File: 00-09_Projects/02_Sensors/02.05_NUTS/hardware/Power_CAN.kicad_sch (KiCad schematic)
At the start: 21 parts, among them J2 USB_C_Receptacle_USB2.0_16P, J3 Conn_01x04_Socket, U1 SN65HVD230, U3 LM3940IMP-3.3/NOPB

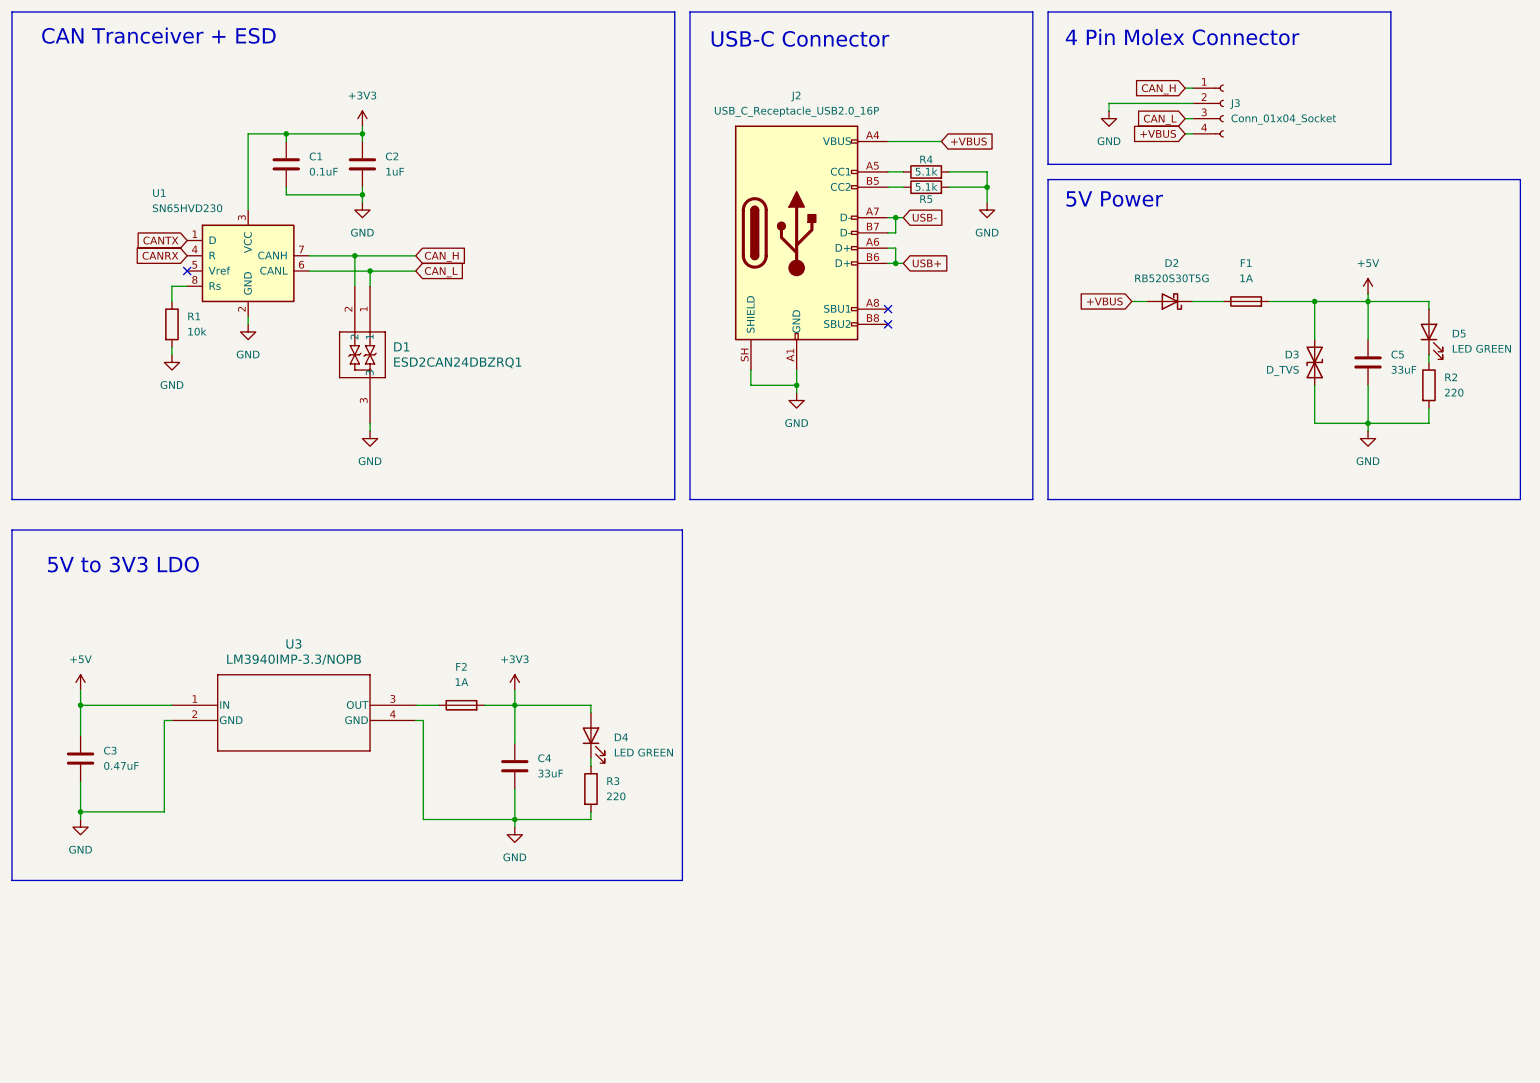
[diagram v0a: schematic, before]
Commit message: Design review changes
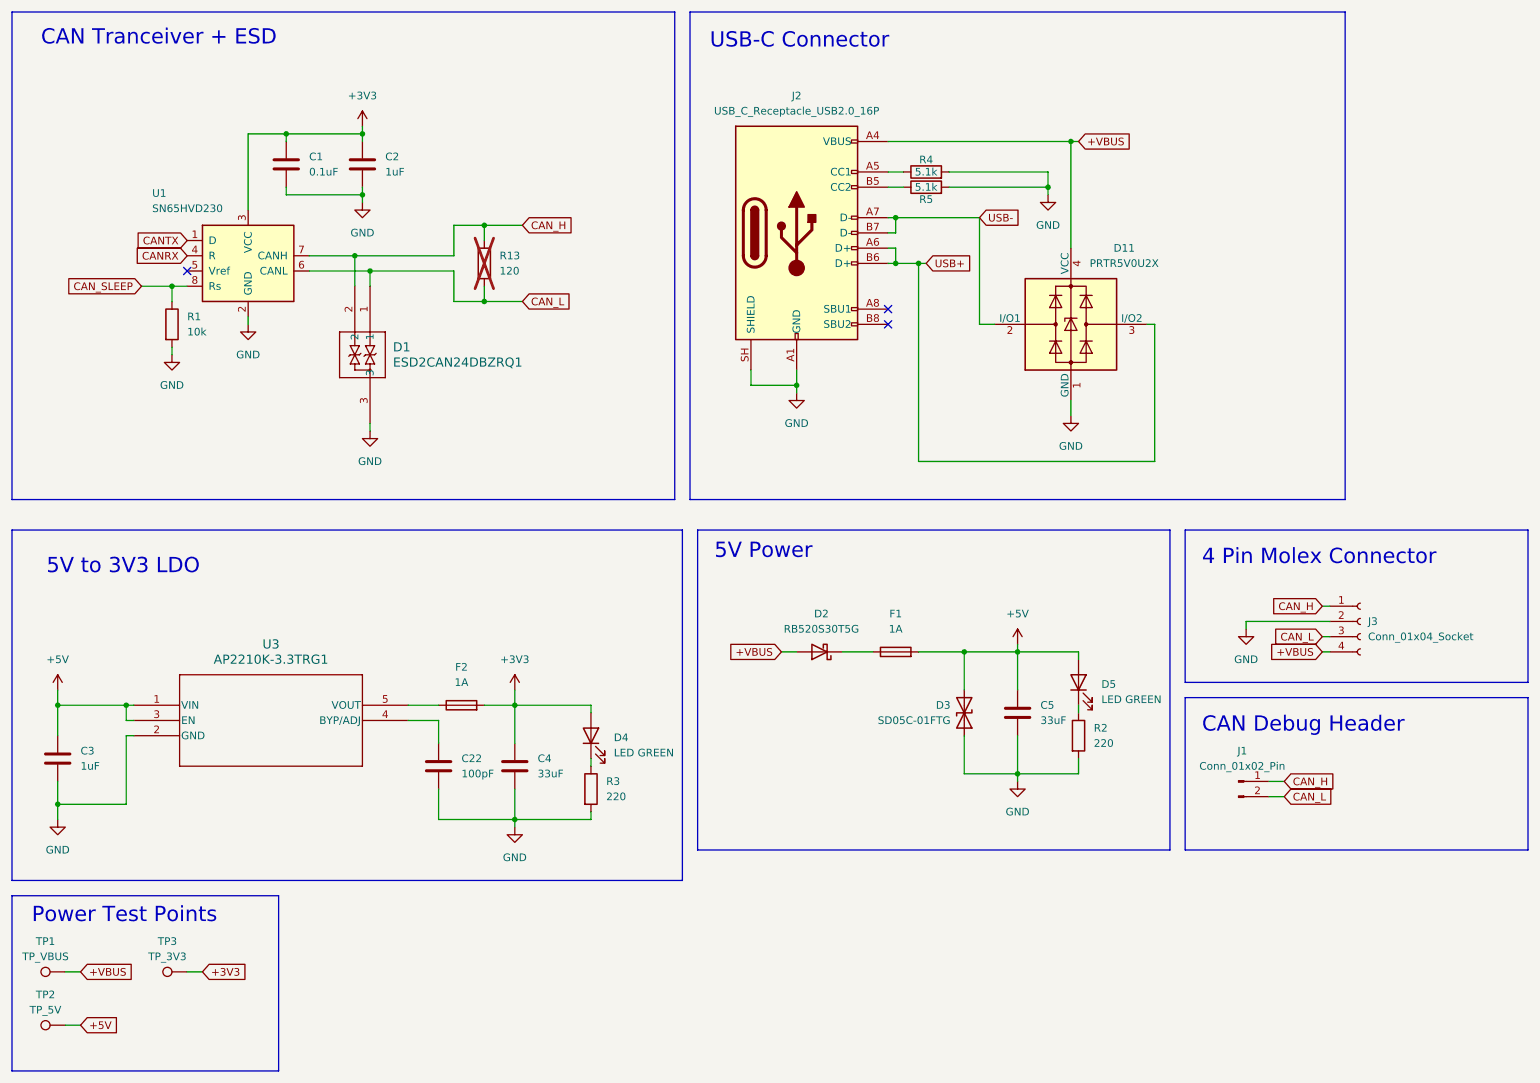
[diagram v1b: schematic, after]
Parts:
- removed U3: LM3940IMP-3.3/NOPB, MP04A, symbol Undertray_Board_sym:LM3940IMP-3.3_NOPB
- added C22: 100pF, Capacitor_SMD:C_0805_2012Metric_Pad1.18x1.45mm_HandSolder, symbol Device:C
- added D11: PRTR5V0U2X, Package_TO_SOT_SMD:SOT-143, symbol Power_Protection:PRTR5V0U2X
- added J1: Conn_01x02_Pin, symbol Connector:Conn_01x02_Pin
- added R13: 120, symbol Device:R
- added TP1: TP_VBUS, symbol Connector:TestPoint
- added TP2: TP_5V, symbol Connector:TestPoint
- added TP3: TP_3V3, symbol Connector:TestPoint
- added U3: AP2210K-3.3TRG1, SOT-23-5_DIO, symbol Undertray_Board_sym:AP2210K-3.3TRG1
- C3: value 0.47uF -> 1uF
- D3: value D_TVS -> SD05C-01FTG
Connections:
- net +3V3: now also TP3.1
- net +5V: now also TP2.1, U3.1 (VIN), U3.3 (EN)
- net +VBUS: now also D11.4 (VCC), TP1.1
- net CAN_H: now also J1.1 (Pin_1), R13.1
- net CAN_L: now also J1.2 (Pin_2), R13.2
- net GND: now also C22.2, D11.1 (GND), U3.2 (GND)
- net USB+: now also D11.3 (I/O2)
- net USB-: now also D11.2 (I/O1)
- net at F2.1: now also U3.5 (VOUT)
- net CAN_SLEEP: now reaches R1.1, U1.8 (Rs)
- new net: C22.1, U3.4 (BYP/ADJ)
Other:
- note added: "CAN Debug Header"
- note added: "Power Test Points"
- moved on the sheet: C3, C5, D2, D3, D5, F1, J3, R2

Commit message: Rev A layout done
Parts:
- removed J1: Conn_01x02_Pin, symbol Connector:Conn_01x02_Pin
- removed J2: USB_C_Receptacle_USB2.0_16P, symbol Connector:USB_C_Receptacle_USB2.0_16P
- added J1: USB_C_Receptacle_USB2.0_16P, Connector_USB:USB_C_Receptacle_XKB_U262-16XN-4BVC11, symbol Connector:USB_C_Receptacle_USB2.0_16P
- D1: footprint SOT-23_DBZ_TEX -> Package_TO_SOT_SMD:SC-59_Handsoldering
- D2: footprint (none) -> Diode_SMD:D_SOD-523
- D3: footprint (none) -> Diode_SMD:D_SOD-323_HandSoldering
- F1, F2: value 1A -> 750mA; footprint (none) -> Fuse:Fuse_1206_3216Metric_Pad1.42x1.75mm_HandSolder
- J3: footprint (none) -> Undertray FP:CONN_SD-43045-001_04_MOL
- R13: footprint (none) -> Resistor_SMD:R_0603_1608Metric_Pad0.98x0.95mm_HandSolder
- TP1, TP2, TP3: footprint (none) -> TestPoint:TestPoint_THTPad_D1.5mm_Drill0.7mm
- U3: footprint SOT-23-5_DIO -> Package_TO_SOT_SMD:SOT-23-5_HandSoldering
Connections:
- net +VBUS: now also J3.2 (Pin_2), J1.A4 (VBUS), J1.A9 (VBUS), J1.B4 (VBUS), J1.B9 (VBUS); no longer J3.4 (Pin_4)
- net CAN_H: now also J3.3 (Pin_3); no longer J3.1 (Pin_1)
- net CAN_L: now also J3.4 (Pin_4); no longer J3.3 (Pin_3)
- net GND: now also J3.1 (Pin_1), J1.A1 (GND), J1.A12 (GND), J1.B1 (GND), J1.B12 (GND), J1.SH (SHIELD); no longer J3.2 (Pin_2)
- net USB+: now also J1.A6 (D+), J1.B6 (D+)
- net USB-: now also J1.A7 (D-), J1.B7 (D-)
- net at R5.1: now also J1.B5 (CC2)
- net at R4.1: now also J1.A5 (CC1)
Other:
- note removed: "CAN Debug Header"

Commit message: Design review rev 1 changes
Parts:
- renumbered C5 to C3, C3 to C4, C22 to C5, C4 to C6, D11 to D2, D2 to D3, D5 to D4, D3 to D5, D4 to D6, J3 to J2, R4 to R1, R5 to R2, R13 to R3, R1 to R4, R2 to R5, R3 to R6, TP3 to TP2, TP2 to TP3, U3 to U2

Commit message: last changes
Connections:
- net +VBUS: now also J2.1 (Pin_1); no longer J2.2 (Pin_2)
- net GND: now also J2.2 (Pin_2); no longer J2.1 (Pin_1)
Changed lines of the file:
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@@
 	(wire
 		(pts
-			(xy 223.52 115.57) (xy 237.49 115.57)
-		)
-		(stroke
-			(width 0)
-			(type default)
-		)
-	)
-	(wire
-		(pts
 			(xy 176.53 137.16) (xy 176.53 143.51)
 		)
@@
 	(wire
 		(pts
-			(xy 236.22 118.11) (xy 237.49 118.11)
-		)
-		(stroke
-			(width 0)
-			(type default)
-		)
-	)
-	(wire
-		(pts
 			(xy 63.5 36.83) (xy 76.2 36.83)
 		)
@@
 	(wire
 		(pts
+			(xy 222.25 118.11) (xy 222.25 119.38)
+		)
+		(stroke
+			(width 0)
+			(type default)
+		)
+	)
+	(wire
+		(pts
 			(xy 25.4 132.08) (xy 36.83 132.08)
 		)
@@
 	(wire
 		(pts
+			(xy 222.25 118.11) (xy 237.49 118.11)
+		)
+		(stroke
+			(width 0)
+			(type default)
+		)
+	)
+	(wire
+		(pts
 			(xy 36.83 134.62) (xy 36.83 132.08)
 		)
@@
 	(wire
 		(pts
-			(xy 223.52 115.57) (xy 223.52 116.84)
-		)
-		(stroke
-			(width 0)
-			(type default)
-		)
-	)
-	(wire
-		(pts
 			(xy 63.5 36.83) (xy 63.5 38.1)
 		)
@@
 	(wire
 		(pts
+			(xy 236.22 115.57) (xy 237.49 115.57)
+		)
+		(stroke
+			(width 0)
+			(type default)
+		)
+	)
+	(wire
+		(pts
 			(xy 101.6 129.54) (xy 101.6 132.08)
 		)
@@
 		)
 	)
-	(global_label "+VBUS"
+	(global_label "CAN_L"
 		(shape input)
-		(at 236.22 118.11 180)
+		(at 236.22 123.19 180)
 		(fields_autoplaced yes)
 		(effects
@@
 		)
 		(property "Intersheetrefs" "${INTERSHEET_REFS}"
-			(at 226.7638 118.11 0)
+			(at 227.55 123.19 0)
 			(hide yes)
 			(show_name no)
@@
 		)
 	)
-	(global_label "CAN_L"
+	(global_label "+VBUS"
 		(shape input)
-		(at 236.22 123.19 180)
+		(at 236.22 115.57 180)
 		(fields_autoplaced yes)
 		(effects
@@
 		)
 		(property "Intersheetrefs" "${INTERSHEET_REFS}"
-			(at 227.55 123.19 0)
+			(at 226.7638 115.57 0)
 			(hide yes)
 			(show_name no)
@@
 	)
 	(symbol
-		(lib_id "power:GND")
-		(at 223.52 116.84 0)
-		(mirror y)
-		(unit 1)
-		(body_style 1)
-		(exclude_from_sim no)
-		(in_bom yes)
-		(on_board yes)
-		(in_pos_files yes)
-		(dnp no)
-		(fields_autoplaced yes)
-		(property "Reference" "#PWR013"
-			(at 223.52 123.19 0)
-			(hide yes)
-			(show_name no)
-			(do_not_autoplace no)
-			(effects
-				(font
-					(size 1.27 1.27)
-				)
-			)
-		)
-		(property "Value" "GND"
-			(at 223.52 121.92 0)
-			(show_name no)
-			(do_not_autoplace no)
-			(effects
-				(font
-					(size 1.27 1.27)
-				)
-			)
-		)
-		(property "Footprint" ""
-			(at 223.52 116.84 0)
-			(hide yes)
-			(show_name no)
-			(do_not_autoplace no)
-			(effects
-				(font
-					(size 1.27 1.27)
-				)
-			)
-		)
-		(property "Datasheet" ""
-			(at 223.52 116.84 0)
-			(hide yes)
-			(show_name no)
-			(do_not_autoplace no)
-			(effects
-				(font
-					(size 1.27 1.27)
-				)
-			)
-		)
-		(property "Description" "Power symbol creates a global label with name \"GND\" , ground"
-			(at 223.52 116.84 0)
-			(hide yes)
-			(show_name no)
-			(do_not_autoplace no)
-			(effects
-				(font
-					(size 1.27 1.27)
-				)
-			)
-		)
-		(pin "1"
-		)
-		(instances
-			(project "Undertray_Board"
-				(path "/85866aa8-1074-44e2-a4f8-fc50fec0cbab/be2888db-2070-4339-a2b3-9cc9a585c76f"
-					(reference "#PWR013")
-					(unit 1)
-				)
-			)
-		)
-	)
-	(symbol
 		(lib_id "Device:C")
 		(at 185.42 133.35 0)
@@
 					(unit 1)
 				)
+			)
+		)
+	)
+	(symbol
+		(lib_id "power:GND")
+		(at 222.25 119.38 0)
+		(mirror y)
+		(unit 1)
+		(body_style 1)
+		(exclude_from_sim no)
+		(in_bom yes)
+		(on_board yes)
+		(in_pos_files yes)
+		(dnp no)
+		(fields_autoplaced yes)
+		(property "Reference" "#PWR013"
+			(at 222.25 125.73 0)
+			(hide yes)
+			(show_name no)
+			(do_not_autoplace no)
+			(effects
+				(font
+					(size 1.27 1.27)
+				)
+			)
+		)
+		(property "Value" "GND"
+			(at 222.25 124.46 0)
+			(show_name no)
+			(do_not_autoplace no)
+			(effects
+				(font
+					(size 1.27 1.27)
+				)
+			)
+		)
+		(property "Footprint" ""
+			(at 222.25 119.38 0)
+			(hide yes)
+			(show_name no)
+			(do_not_autoplace no)
+			(effects
+				(font
+					(size 1.27 1.27)
+				)
+			)
+		)
+		(property "Datasheet" ""
+			(at 222.25 119.38 0)
+			(hide yes)
+			(show_name no)
+			(do_not_autoplace no)
+			(effects
+				(font
+					(size 1.27 1.27)
+				)
+			)
+		)
+		(property "Description" "Power symbol creates a global label with name \"GND\" , ground"
+			(at 222.25 119.38 0)
+			(hide yes)
+			(show_name no)
+			(do_not_autoplace no)
+			(effects
+				(font
+					(size 1.27 1.27)
+				)
+			)
+		)
+		(pin "1"
+		)
+		(instances
+			(project "Undertray_Board"
+				(path "/85866aa8-1074-44e2-a4f8-fc50fec0cbab/be2888db-2070-4339-a2b3-9cc9a585c76f"
+					(reference "#PWR013")
+					(unit 1)
+				)

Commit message: extra changes
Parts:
- R5, R6: value 220 -> 330
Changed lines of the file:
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@@
 			)
 		)
-		(property "Value" "220"
+		(property "Value" "330"
 			(at 198.12 138.4299 0)
 			(show_name no)
@@
 			)
 		)
-		(property "Value" "220"
+		(property "Value" "330"
 			(at 116.84 147.3199 0)
 			(show_name no)

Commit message: solder jumper for reset
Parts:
- D3: value RB520S30T5G -> SDM20U30-7
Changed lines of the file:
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@@
 			)
 		)
-		(property "Value" "RB520S30T5G"
+		(property "Value" "SDM20U30-7"
 			(at 152.7175 119.38 0)
 			(show_name no)

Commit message: usb D+ pull up res fix
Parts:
- added R20: 1.5k, Resistor_SMD:R_0603_1608Metric_Pad0.98x0.95mm_HandSolder, symbol Device:R
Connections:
- net +3V3: now also R20.1
- net USB+: now also R20.2
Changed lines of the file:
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@@
 	)
 	(junction
+		(at 195.58 123.19)
+		(diameter 0)
+		(color 0 0 0 0)
+	)
+	(junction
 		(at 76.2 36.83)
 		(diameter 0)
@@
 	)
 	(junction
+		(at 214.63 68.58)
+		(diameter 0)
+		(color 0 0 0 0)
+	)
+	(junction
 		(at 25.4 148.59)
 		(diameter 0)
@@
 	)
 	(junction
-		(at 168.91 58.42)
+		(at 44.45 62.23)
 		(diameter 0)
 		(color 0 0 0 0)
 	)
 	(junction
-		(at 44.45 62.23)
+		(at 148.59 78.74)
 		(diameter 0)
 		(color 0 0 0 0)
 	)
 	(junction
-		(at 148.59 78.74)
+		(at 195.58 143.51)
 		(diameter 0)
 		(color 0 0 0 0)
@@
 	(wire
 		(pts
+			(xy 195.58 143.51) (xy 185.42 143.51)
+		)
+		(stroke
+			(width 0)
+			(type default)
+		)
+	)
+	(wire
+		(pts
 			(xy 38.1 134.62) (xy 36.83 134.62)
 		)
@@
 	(wire
 		(pts
-			(xy 208.28 68.58) (xy 207.01 68.58)
+			(xy 214.63 68.58) (xy 207.01 68.58)
 		)
 		(stroke
@@
 	(wire
 		(pts
-			(xy 185.42 144.78) (xy 185.42 143.51)
+			(xy 214.63 66.04) (xy 214.63 68.58)
 		)
 		(stroke
@@
 	(wire
 		(pts
-			(xy 25.4 144.78) (xy 25.4 148.59)
+			(xy 195.58 144.78) (xy 195.58 143.51)
 		)
 		(stroke
@@
 	(wire
 		(pts
-			(xy 38.1 137.16) (xy 36.83 137.16)
+			(xy 25.4 144.78) (xy 25.4 148.59)
 		)
 		(stroke
@@
 	(wire
 		(pts
-			(xy 170.18 58.42) (xy 168.91 58.42)
+			(xy 38.1 137.16) (xy 36.83 137.16)
 		)
 		(stroke
@@
 	(wire
 		(pts
-			(xy 208.28 91.44) (xy 168.91 91.44)
+			(xy 214.63 91.44) (xy 168.91 91.44)
 		)
 		(stroke
@@
 	(wire
 		(pts
+			(xy 214.63 54.61) (xy 214.63 58.42)
+		)
+		(stroke
+			(width 0)
+			(type default)
+		)
+	)
+	(wire
+		(pts
 			(xy 146.05 123.19) (xy 148.59 123.19)
 		)
@@
 	(wire
 		(pts
-			(xy 195.58 132.08) (xy 195.58 133.35)
+			(xy 214.63 68.58) (xy 215.9 68.58)
 		)
 		(stroke
@@
 	(wire
 		(pts
-			(xy 195.58 143.51) (xy 185.42 143.51)
+			(xy 195.58 132.08) (xy 195.58 133.35)
 		)
 		(stroke
@@
 	(wire
 		(pts
-			(xy 185.42 121.92) (xy 185.42 123.19)
+			(xy 195.58 120.65) (xy 195.58 123.19)
 		)
 		(stroke
@@
 	(wire
 		(pts
-			(xy 208.28 68.58) (xy 208.28 91.44)
+			(xy 214.63 68.58) (xy 214.63 91.44)
 		)
 		(stroke
@@
 		)
 	)
-	(global_label "USB+"
-		(shape input)
-		(at 170.18 58.42 0)
-		(fields_autoplaced yes)
-		(effects
-			(font
-				(size 1.27 1.27)
-			)
-			(justify left)
-		)
-		(property "Intersheetrefs" "${INTERSHEET_REFS}"
-			(at 178.5476 58.42 0)
-			(hide yes)
-			(show_name no)
-			(do_not_autoplace no)
-			(effects
-				(font
-					(size 1.27 1.27)
-				)
-				(justify left)
-			)
-		)
-	)
 	(global_label "CAN_SLEEP"
 		(shape input)
@@
 		)
 	)
+	(global_label "USB+"
+		(shape input)
+		(at 215.9 68.58 0)
+		(fields_autoplaced yes)
+		(effects
+			(font
+				(size 1.27 1.27)
+			)
+			(justify left)
+		)
+		(property "Intersheetrefs" "${INTERSHEET_REFS}"
+			(at 224.2676 68.58 0)
+			(hide yes)
+			(show_name no)
+			(do_not_autoplace no)
+			(effects
+				(font
+					(size 1.27 1.27)
+				)
+				(justify left)
+			)
+		)
+	)
 	(global_label "+VBUS"
 		(shape input)
@@
 	(symbol
 		(lib_id "power:+5V")
-		(at 185.42 121.92 0)
+		(at 195.58 120.65 0)
 		(mirror y)
 		(unit 1)
@@
 		(fields_autoplaced yes)
 		(property "Reference" "#PWR014"
-			(at 185.42 125.73 0)
+			(at 195.58 124.46 0)
 			(hide yes)
 			(show_name no)
@@
 		)
 		(property "Value" "+5V"
-			(at 185.42 116.84 0)
+			(at 195.58 115.57 0)
 			(show_name no)
 			(do_not_autoplace no)
@@
 		)
 		(property "Footprint" ""
-			(at 185.42 121.92 0)
+			(at 195.58 120.65 0)
 			(hide yes)
 			(show_name no)
@@
 		)
 		(property "Datasheet" ""
-			(at 185.42 121.92 0)
+			(at 195.58 120.65 0)
 			(hide yes)
 			(show_name no)
@@
 		)
 		(property "Description" "Power symbol creates a global label with name \"+5V\""
-			(at 185.42 121.92 0)
+			(at 195.58 120.65 0)
 			(hide yes)
 			(show_name no)
@@
 	)
 	(symbol
+		(lib_id "Device:R")
+		(at 214.63 62.23 0)
+		(unit 1)
+		(body_style 1)
+		(exclude_from_sim no)
+		(in_bom yes)
+		(on_board yes)
+		(in_pos_files yes)
+		(dnp no)
+		(fields_autoplaced yes)
+		(property "Reference" "R20"
+			(at 217.17 60.9599 0)
+			(show_name no)
+			(do_not_autoplace no)
+			(effects
+				(font
+					(size 1.27 1.27)
+				)
+				(justify left)
+			)
+		)
+		(property "Value" "1.5k"
+			(at 217.17 63.4999 0)
+			(show_name no)
+			(do_not_autoplace no)
+			(effects
+				(font
+					(size 1.27 1.27)
+				)
+				(justify left)
+			)
+		)
+		(property "Footprint" "Resistor_SMD:R_0603_1608Metric_Pad0.98x0.95mm_HandSolder"
+			(at 212.852 62.23 90)
+			(hide yes)
+			(show_name no)
+			(do_not_autoplace no)
+			(effects
+				(font
+					(size 1.27 1.27)
+				)
+			)
+		)
+		(property "Datasheet" ""
+			(at 214.63 62.23 0)
+			(hide yes)
+			(show_name no)
+			(do_not_autoplace no)
+			(effects
+				(font
+					(size 1.27 1.27)
+				)
+			)
+		)
+		(property "Description" "Resistor"
+			(at 214.63 62.23 0)
+			(hide yes)
+			(show_name no)
+			(do_not_autoplace no)
+			(effects
+				(font
+					(size 1.27 1.27)
+				)
+			)
+		)
+		(pin "2"
+		)
+		(pin "1"
+		)
+		(instances
+			(project "Undertray_Board"
+				(path "/85866aa8-1074-44e2-a4f8-fc50fec0cbab/be2888db-2070-4339-a2b3-9cc9a585c76f"
+					(reference "R20")
+					(unit 1)
+				)
+			)
+		)
+	)
+	(symbol
 		(lib_id "power:GND")
-		(at 185.42 144.78 0)
+		(at 195.58 144.78 0)
 		(mirror y)
 		(unit 1)
@@
 		(fields_autoplaced yes)
 		(property "Reference" "#PWR017"
-			(at 185.42 151.13 0)
+			(at 195.58 151.13 0)
 			(hide yes)
 			(show_name no)
@@
 		)
 		(property "Value" "GND"
-			(at 185.42 149.86 0)
+			(at 195.58 149.86 0)
 			(show_name no)
 			(do_not_autoplace no)
@@
 		)
 		(property "Footprint" ""
-			(at 185.42 144.78 0)
+			(at 195.58 144.78 0)
 			(hide yes)
 			(show_name no)
@@
 		)
 		(property "Datasheet" ""
-			(at 185.42 144.78 0)
+			(at 195.58 144.78 0)
 			(hide yes)
 			(show_name no)
@@
 		)
 		(property "Description" "Power symbol creates a global label with name \"GND\" , ground"
-			(at 185.42 144.78 0)
+			(at 195.58 144.78 0)
 			(hide yes)
 			(show_name no)
@@
 					(unit 1)
 				)
+			)
+		)
+	)
+	(symbol
+		(lib_id "power:+3V3")
+		(at 214.63 54.61 0)
+		(unit 1)
+		(body_style 1)
+		(exclude_from_sim no)
+		(in_bom yes)
+		(on_board yes)
+		(in_pos_files yes)
+		(dnp no)
+		(fields_autoplaced yes)
+		(property "Reference" "#PWR062"
+			(at 214.63 58.42 0)
+			(hide yes)
+			(show_name no)
+			(do_not_autoplace no)
+			(effects
+				(font
+					(size 1.27 1.27)
+				)
+			)
+		)
+		(property "Value" "+3V3"
+			(at 214.63 49.53 0)
+			(show_name no)
+			(do_not_autoplace no)
+			(effects
+				(font
+					(size 1.27 1.27)
+				)
+			)
+		)
+		(property "Footprint" ""
+			(at 214.63 54.61 0)
+			(hide yes)
+			(show_name no)
+			(do_not_autoplace no)
+			(effects
+				(font
+					(size 1.27 1.27)
+				)
+			)
+		)
+		(property "Datasheet" ""
+			(at 214.63 54.61 0)
+			(hide yes)
+			(show_name no)
+			(do_not_autoplace no)
+			(effects
+				(font
+					(size 1.27 1.27)
+				)
+			)
+		)
+		(property "Description" "Power symbol creates a global label with name \"+3V3\""
+			(at 214.63 54.61 0)
+			(hide yes)
+			(show_name no)
+			(do_not_autoplace no)
+			(effects
+				(font
+					(size 1.27 1.27)
+				)
+			)
+		)
+		(pin "1"
+		)
+		(instances
+			(project "Undertray_Board"
+				(path "/85866aa8-1074-44e2-a4f8-fc50fec0cbab/be2888db-2070-4339-a2b3-9cc9a585c76f"
+					(reference "#PWR062")
+					(unit 1)
+				)
